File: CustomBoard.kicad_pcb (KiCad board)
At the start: 2 copper layers, 32.9 x 32.8 mm, 25 parts, among them J1 RIGHT, J10 Sensor08, J11 Sensor09, J12 Sensor10, J13 Sensor11, J14 Sensor12, J15 Sensor13, J16 Sensor14, J17 TEST_1P, J2 LEFT, J3 Sensor01, J4 Sensor02, J5 Sensor03, J6 Sensor04, J7 Sensor05, J8 Sensor06, J9 Sensor07, U1 DS28E05, U2 PCA9555

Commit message: 4m range ToF sensor parts
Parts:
- removed G***: OUTLINE, board_outlines:TMP_THICK_BASE

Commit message: new footprints
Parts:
- removed J15: Sensor13, footprint:SensorPads
- removed J16: Sensor14, footprint:SensorPads
- removed J17: TEST_1P, Measurement_Points:Measurement_Point_Round-SMD-Pad_Small
- removed R2, R3: 10k, Resistors_SMD:R_0603
- added C2: 100n, Capacitors_SMD:C_0402, F.Cu at (146.1, 117.6)
- added C3: 4.7u, Capacitors_SMD:C_0402, F.Cu at (151.9, 117.6)
- added R4: 10k, Resistors_SMD:R_0402, F.Cu at (149.0, 112.4)
- added U3: VL53L1X, footprint:VL53L1X, F.Cu at (148.2, 117.6)
- C1: value PowerC -> 100n; footprint Capacitors_SMD:C_0603 -> Capacitors_SMD:C_0402; moved to B.Cu
- D1: footprint LEDs:LED_0603 -> LEDs:LED_0402
- J1: footprint Pin_Headers:Pin_Header_Straight_1x10_Pitch2.00mm_SMD_Pin1Right -> Pin_Header_Straight_1x10_Pitch2.00mm_SMD_Pin1Right; moved to F.Cu
- J2: footprint Pin_Headers:Pin_Header_Straight_1x10_Pitch2.00mm_SMD_Pin1Left -> Pin_Header_Straight_1x10_Pitch2.00mm_SMD_Pin1Left; moved to F.Cu
- R1: footprint Resistors_SMD:R_0603 -> Resistors_SMD:R_0402; moved to B.Cu
- U1, U2: moved to B.Cu
- moved J12 14.6 mm to (165.4, 114.8), turned to 90 degrees
- moved J11 13.6 mm to (165.9, 122.4), turned to 90 degrees
- moved J13 12.5 mm to (165.7, 108.1)
- moved J10 12.2 mm to (161.9, 130.4)
- moved J14 9.84 mm to (162.2, 102.7), turned to 0 degrees
- moved J5 8.35 mm to (132.1, 110.7), turned to 90 degrees
- moved J4 7.30 mm to (135.9, 102.8), turned to 0 degrees
- moved J6 5.70 mm to (132.1, 117.2), turned to 90 degrees
- moved J9 5.45 mm to (148.8, 132.6)
- moved J7 4.40 mm to (132.0, 124.5)
- moved J8 1.57 mm to (136.4, 130.7), turned to 0 degrees
- moved J3 0.86 mm to (150.3, 100.6)
- turned C1 to 90 degrees
- turned R1 to 90 degrees
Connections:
- net WKUP/OW renamed OW
- U2 pad 17: TEST -> S15
- U2 pad 18: Net-(R3-Pad1) -> GND
- U2 pad 22: Net-(R2-Pad1) -> (no net)
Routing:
- net GND: track 126.5 -> 19.4 mm, vias 14 -> 0
- net S01: track 24.5 -> 0.00 mm
- net S13: track 21.3 -> 0.00 mm
- net S03: track 21.0 -> 0.00 mm
- net S02: track 21.0 -> 0.00 mm
- net S14: track 20.2 -> 0.00 mm
- net S10: track 18.8 -> 0.00 mm
- net S06: track 17.3 -> 0.00 mm
- net S07: track 16.3 -> 0.00 mm
- net S04: track 16.3 -> 0.00 mm
- net S09: track 16.2 -> 0.00 mm
- net S11: track 15.7 -> 0.00 mm
- net S12: track 15.6 -> 0.00 mm
- net S05: track 14.8 -> 0.00 mm
- net S08: track 14.1 -> 0.00 mm
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
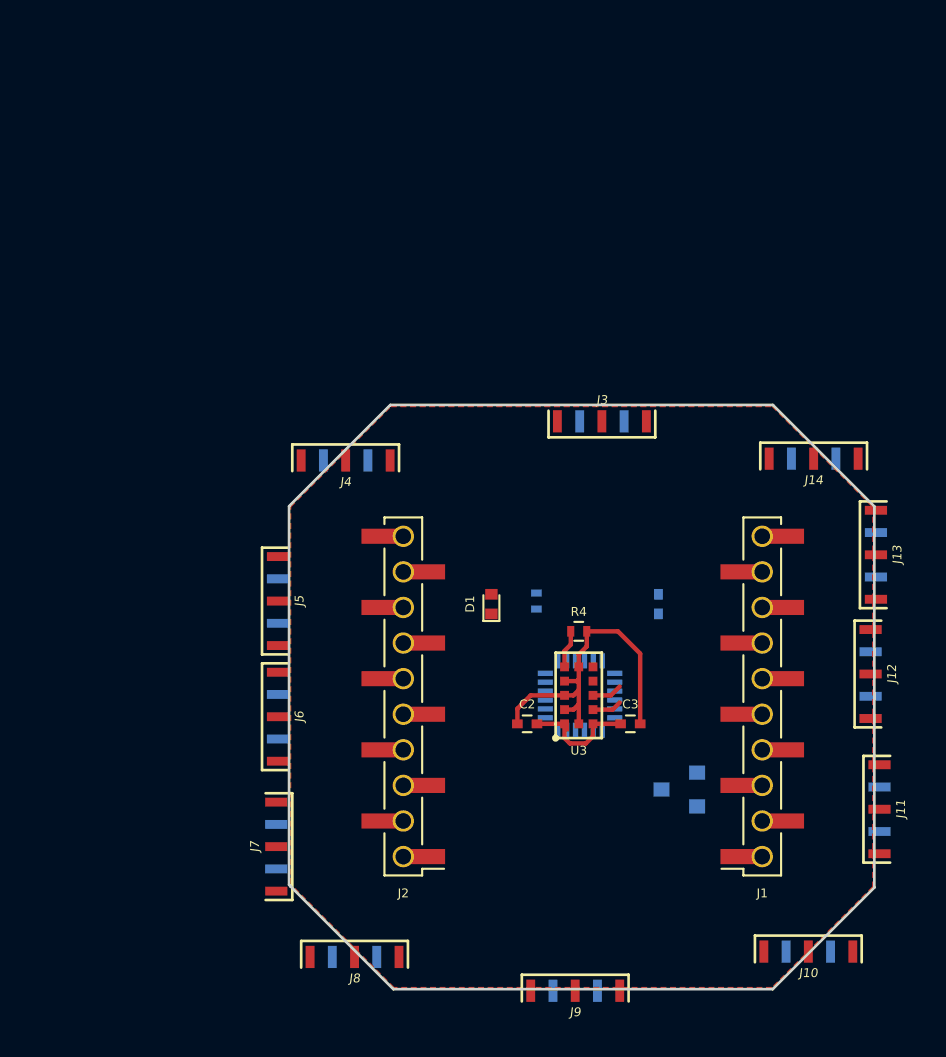
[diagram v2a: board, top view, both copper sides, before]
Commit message: dimensions fixed
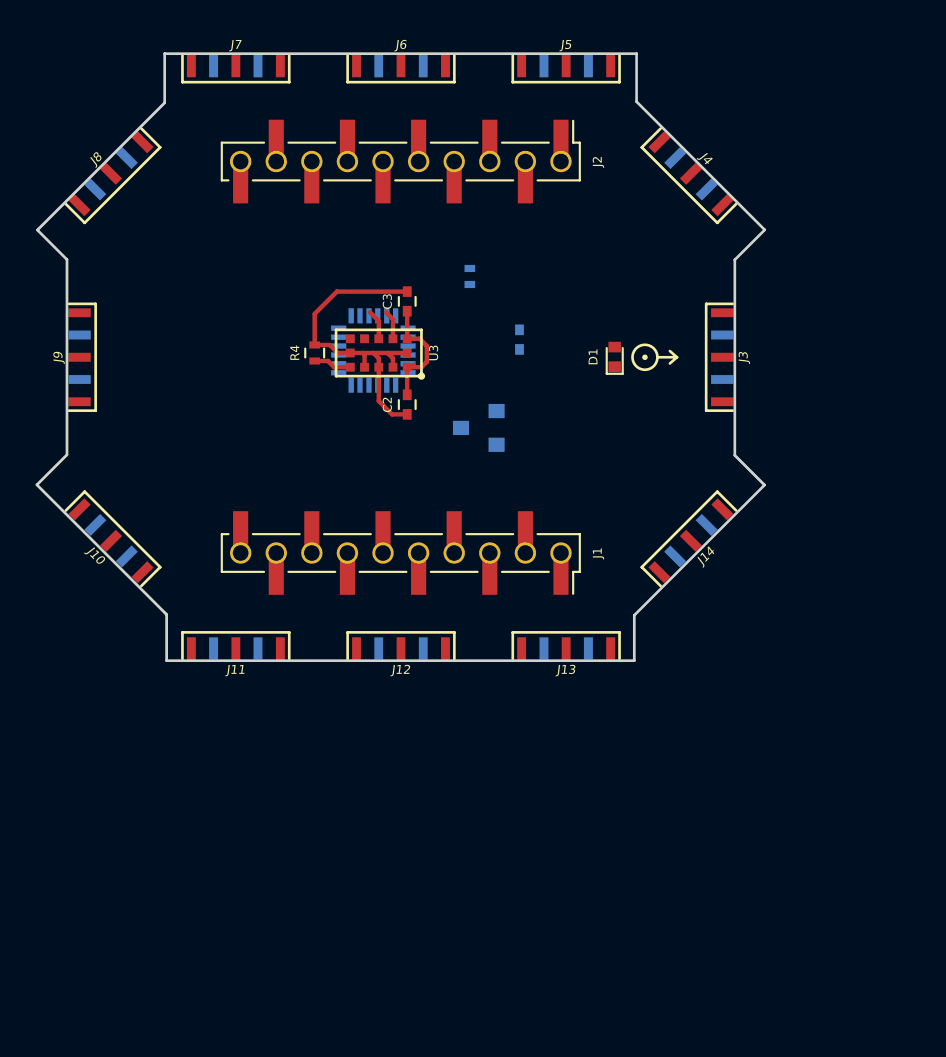
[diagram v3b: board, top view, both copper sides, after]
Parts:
- added EXP_ORIENTATION: VAL**, crazy2libs:EXP_ORIENTATION, F.Cu at (152.7, 97.0)
- moved J8 46.1 mm to (122.7, 86.7), turned to 225 degrees
- moved J10 45.5 mm to (122.7, 107.3), turned to 315 degrees
- moved J9 45.2 mm to (121.0, 97.0), turned to 270 degrees
- moved J7 43.9 mm to (129.7, 80.6), turned to 180 degrees
- moved J11 37.3 mm to (129.7, 113.4), turned to 0 degrees
- moved J6 37.2 mm to (139.0, 80.6), turned to 180 degrees
- moved J5 34.1 mm to (148.3, 80.6), turned to 180 degrees
- moved J2 30.1 mm to (139.0, 86.0), turned to 270 degrees
- moved C3 26.8 mm to (139.4, 93.9), turned to 90 degrees
- moved J12 26.4 mm to (139.0, 113.4), turned to 0 degrees
- moved J4 25.2 mm to (155.3, 86.7), turned to 135 degrees
- moved U1 23.2 mm to (143.4, 101.0)
- moved U2 22.6 mm to (137.5, 96.6)
- moved U3 21.9 mm to (139.4, 97.6), turned to 90 degrees
- moved J1 21.9 mm to (139.0, 108.0), turned to 270 degrees
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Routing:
- removed copper zone on F.Cu, net GND
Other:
- board size 32.9 x 32.8 mm -> 40.9 x 34.1 mm

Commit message: routing started
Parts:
- J1, J2: moved to B.Cu
- moved C1 17.8 mm to (127.9, 95.2), turned to 270 degrees
- moved U1 12.6 mm to (131.0, 102.9), turned to 90 degrees
- moved R1 8.43 mm to (151.0, 94.7), turned to 270 degrees
- moved U2 5.26 mm to (132.2, 97.0), turned to 180 degrees
- turned J1 to 90 degrees
- turned J2 to 90 degrees
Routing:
- net SCL: track 1.67 -> 149.9 mm, vias 0 -> 2
- net SDA: track 1.71 -> 22.0 mm, vias 0 -> 1
- net Net-(D1-Pad1): track 0.00 -> 17.6 mm, vias 0 -> 1
- net S15: track 2.14 -> 13.5 mm, vias 0 -> 1
- net VCC: track 6.49 -> 17.0 mm
- net GND: track 19.4 -> 25.3 mm
- net OW: track 0.00 -> 5.72 mm
- net Net-(D1-Pad2): track 0.00 -> 4.30 mm, vias 0 -> 1

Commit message: routing continues
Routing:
- net SDA: track 22.0 -> 118.1 mm
- net GND: track 25.3 -> 40.7 mm, vias 0 -> 1
- net SCL: track 149.9 -> 154.5 mm
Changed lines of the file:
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@@
   (general
     (links 96)
-    (no_connects 58)
+    (no_connects 53)
     (area 118.474999 79.864999 159.525001 114.125001)
     (thickness 0.8)
     (drawings 18023)
-    (tracks 124)
+    (tracks 157)
     (zones 0)
     (modules 24)
@@
   (gr_line (start 183.551 150.189) (end 175.849 152.992) (layer Eco1.User) (width 0.1))
   (gr_line (start 189.83 144.921) (end 183.551 150.189) (layer Eco1.User) (width 0.1))
+  (segment (start 132.23 80.64) (end 132.23 83.34) (width 0.25) (layer F.Cu) (net 1))
+  (segment (start 130.745 84.825) (end 130 84.825) (width 0.25) (layer B.Cu) (net 1))
+  (segment (start 132.23 83.34) (end 130.745 84.825) (width 0.25) (layer B.Cu) (net 1))
+  (via (at 132.23 83.34) (size 0.6) (drill 0.4) (layers F.Cu B.Cu) (net 1))
+  (segment (start 124.487767 84.922233) (end 124.487767 84.927767) (width 0.25) (layer F.Cu) (net 1))
+  (segment (start 124.487767 84.927767) (end 125.56 86) (width 0.25) (layer F.Cu) (net 1))
+  (segment (start 125.56 86) (end 130 86) (width 0.25) (layer F.Cu) (net 1))
+  (segment (start 130.96 101.88) (end 131.49 101.88) (width 0.25) (layer B.Cu) (net 1))
+  (segment (start 132.46 100.91) (end 132.46 98.9) (width 0.25) (layer B.Cu) (net 1))
+  (segment (start 131.49 101.88) (end 132.46 100.91) (width 0.25) (layer B.Cu) (net 1))
   (segment (start 132.96 95) (end 132.96 93.52) (width 0.25) (layer B.Cu) (net 1))
   (segment (start 133.46 93.51) (end 133.46 95) (width 0.25) (layer B.Cu) (net 1))
@@
   (via (at 149.08 97.54) (size 0.6) (drill 0.4) (layers F.Cu B.Cu) (net 4))
   (segment (start 147.24 95.7) (end 149.08 97.54) (width 0.25) (layer B.Cu) (net 4))
-  (segment (start 137.76 95.96) (end 137.76 95) (width 0.25) (layer F.Cu) (net 5) (status 400000))
+  (segment (start 128.415 108.765) (end 128.415 107.245) (width 0.25) (layer F.Cu) (net 5))
+  (segment (start 128.415 107.245) (end 124.88 103.71) (width 0.25) (layer F.Cu) (net 5))
+  (segment (start 122.72 86.69) (end 124.88 88.85) (width 0.25) (layer F.Cu) (net 5))
+  (segment (start 124.88 88.85) (end 124.88 103.71) (width 0.25) (layer F.Cu) (net 5))
+  (segment (start 129.73 83.67) (end 129.73 80.64) (width 0.25) (layer F.Cu) (net 5))
+  (segment (start 130.45 84.39) (end 129.73 83.67) (width 0.25) (layer F.Cu) (net 5))
+  (segment (start 148.57 84.39) (end 130.45 84.39) (width 0.25) (layer F.Cu) (net 5))
+  (segment (start 149.46 85.28) (end 148.57 84.39) (width 0.25) (layer F.Cu) (net 5))
+  (segment (start 149.46 86.32) (end 149.46 85.28) (width 0.25) (layer F.Cu) (net 5))
+  (segment (start 153.06 89.92) (end 149.46 86.32) (width 0.25) (layer F.Cu) (net 5))
+  (segment (start 153.06 103.48) (end 153.06 89.92) (width 0.25) (layer F.Cu) (net 5))
+  (segment (start 149.63 106.91) (end 153.06 103.48) (width 0.25) (layer F.Cu) (net 5))
+  (segment (start 149.63 108.62) (end 149.63 106.91) (width 0.25) (layer F.Cu) (net 5))
+  (segment (start 148.79 109.46) (end 149.63 108.62) (width 0.25) (layer F.Cu) (net 5))
+  (segment (start 129.11 109.46) (end 148.79 109.46) (width 0.25) (layer F.Cu) (net 5))
+  (segment (start 128.415 108.765) (end 129.11 109.46) (width 0.25) (layer F.Cu) (net 5))
+  (segment (start 122.72 107.31) (end 122.72 107.27) (width 0.25) (layer F.Cu) (net 5))
+  (segment (start 155.3 107.31) (end 155.27 107.31) (width 0.25) (layer F.Cu) (net 5))
+  (segment (start 155.3 86.69) (end 155.29 86.69) (width 0.25) (layer F.Cu) (net 5))
+  (segment (start 137.76 95.96) (end 137.76 95) (width 0.25) (layer F.Cu) (net 5))
   (segment (start 135.62 92.86) (end 135.62 92.09) (width 0.25) (layer B.Cu) (net 5))
   (segment (start 137.25 94.49) (end 135.62 92.86) (width 0.25) (layer B.Cu) (net 5))
@@
   (segment (start 135.62 92.09) (end 132.38 92.09) (width 0.25) (layer B.Cu) (net 5))
   (segment (start 142 89.11) (end 139.02 92.09) (width 0.25) (layer B.Cu) (net 5))
-  (segment (start 138.56 95.96) (end 138.56 94.72) (width 0.25) (layer F.Cu) (net 6) (status 400000))
-  (segment (start 140 92.17) (end 140 86) (width 0.25) (layer F.Cu) (net 6) (status 800000))
+  (segment (start 140 87.175) (end 140 82.74) (width 0.25) (layer B.Cu) (net 6))
+  (segment (start 140 82.74) (end 139.73 82.47) (width 0.25) (layer B.Cu) (net 6))
+  (segment (start 147.04 80.64) (end 147.04 81.84) (width 0.25) (layer B.Cu) (net 6))
+  (segment (start 147.04 81.84) (end 147.67 82.47) (width 0.25) (layer B.Cu) (net 6))
+  (segment (start 137.76 80.64) (end 137.76 82.02) (width 0.25) (layer B.Cu) (net 6))
+  (segment (start 137.76 82.02) (end 138.21 82.47) (width 0.25) (layer B.Cu) (net 6))
+  (segment (start 128.48 80.64) (end 128.48 82.19) (width 0.25) (layer B.Cu) (net 6))
+  (segment (start 148.74 82.47) (end 148.89 82.62) (width 0.25) (layer B.Cu) (net 6))
+  (segment (start 128.76 82.47) (end 138.21 82.47) (width 0.25) (layer B.Cu) (net 6))
+  (segment (start 138.21 82.47) (end 139.73 82.47) (width 0.25) (layer B.Cu) (net 6))
+  (segment (start 139.73 82.47) (end 147.67 82.47) (width 0.25) (layer B.Cu) (net 6))
+  (segment (start 147.67 82.47) (end 148.74 82.47) (width 0.25) (layer B.Cu) (net 6))
+  (segment (start 128.48 82.19) (end 128.76 82.47) (width 0.25) (layer B.Cu) (net 6))
+  (segment (start 157.06 95.75) (end 155.64 95.75) (width 0.25) (layer B.Cu) (net 6))
+  (segment (start 155.64 95.75) (end 155.37 95.48) (width 0.25) (layer B.Cu) (net 6))
+  (segment (start 138.56 95.96) (end 138.56 94.72) (width 0.25) (layer F.Cu) (net 6))
+  (segment (start 140 92.17) (end 140 86) (width 0.25) (layer F.Cu) (net 6))
   (via (at 140 92.17) (size 0.6) (drill 0.4) (layers F.Cu B.Cu) (net 6))
   (segment (start 140 92.84) (end 140 92.17) (width 0.25) (layer B.Cu) (net 6))
@@
   (segment (start 156.183883 106.426117) (end 156.166117 106.426117) (width 0.25) (layer B.Cu) (net 6))
   (segment (start 156.166117 106.426117) (end 154.89 105.15) (width 0.25) (layer B.Cu) (net 6))
-  (segment (start 157.06 95.75) (end 155.64 95.75) (width 0.25) (layer B.Cu) (net 6))
-  (segment (start 155.64 95.75) (end 155.37 95.48) (width 0.25) (layer B.Cu) (net 6))
   (segment (start 154.416117 85.806117) (end 154.413883 85.806117) (width 0.25) (layer B.Cu) (net 6))
   (segment (start 154.413883 85.806117) (end 153.245 86.975) (width 0.25) (layer B.Cu) (net 6))
-  (segment (start 147.04 80.64) (end 147.04 82.24) (width 0.25) (layer B.Cu) (net 6))
-  (segment (start 147.04 82.24) (end 147.42 82.62) (width 0.25) (layer B.Cu) (net 6))
-  (segment (start 137.76 80.64) (end 137.76 82.19) (width 0.25) (layer B.Cu) (net 6))
-  (segment (start 137.76 82.19) (end 138.19 82.62) (width 0.25) (layer B.Cu) (net 6))
   (segment (start 120.95 98.25) (end 122.51 98.25) (width 0.25) (layer B.Cu) (net 6))
   (segment (start 122.51 98.25) (end 122.68 98.42) (width 0.25) (layer B.Cu) (net 6))
   (segment (start 123.603883 108.193883) (end 123.603883 108.186117) (width 0.25) (layer B.Cu) (net 6))
   (segment (start 123.603883 108.186117) (end 124.83 106.96) (width 0.25) (layer B.Cu) (net 6))
-  (segment (start 128.48 80.64) (end 128.48 82.25) (width 0.25) (layer B.Cu) (net 6))
   (segment (start 122.68 88.417766) (end 121.836117 87.573883) (width 0.25) (layer B.Cu) (net 6))
   (segment (start 122.68 104.81) (end 122.68 98.42) (width 0.25) (layer B.Cu) (net 6))
@@
   (segment (start 148.89 82.62) (end 153.245 86.975) (width 0.25) (layer B.Cu) (net 6))
   (segment (start 153.245 86.975) (end 155.37 89.1) (width 0.25) (layer B.Cu) (net 6))
-  (segment (start 128.85 82.62) (end 138.19 82.62) (width 0.25) (layer B.Cu) (net 6))
-  (segment (start 138.19 82.62) (end 147.42 82.62) (width 0.25) (layer B.Cu) (net 6))
-  (segment (start 147.42 82.62) (end 148.89 82.62) (width 0.25) (layer B.Cu) (net 6))
-  (segment (start 128.48 82.25) (end 128.85 82.62) (width 0.25) (layer B.Cu) (net 6))
   (segment (start 130.96 95) (end 130.96 92.69) (width 0.25) (layer B.Cu) (net 6))
   (segment (start 140 90.15) (end 140 86) (width 0.25) (layer B.Cu) (net 6))
@@
   (segment (start 134 104.72) (end 134 108) (width 0.25) (layer B.Cu) (net 21))
   (segment (start 133.16 103.88) (end 134 104.72) (width 0.25) (layer B.Cu) (net 21))
-  (segment (start 130.26 96.2) (end 128.81 96.2) (width 0.25) (layer B.Cu) (net 22) (status 400000))
-  (segment (start 133.64 97.21) (end 134.16 97.21) (width 0.25) (layer F.Cu) (net 22) (status 800000))
+  (segment (start 130.26 96.2) (end 128.81 96.2) (width 0.25) (layer B.Cu) (net 22))
+  (segment (start 133.64 97.21) (end 134.16 97.21) (width 0.25) (layer F.Cu) (net 22))
   (segment (start 132.63 96.2) (end 133.64 97.21) (width 0.25) (layer F.Cu) (net 22))
   (segment (start 127.53 96.2) (end 132.63 96.2) (width 0.25) (layer F.Cu) (net 22))

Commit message: routing optimization
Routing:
- net VCC: track 17.0 -> 99.8 mm, vias 0 -> 21
- net GND: track 40.7 -> 118.5 mm, vias 1 -> 22
- net SDA: track 118.1 -> 160.3 mm
- net S07: track 0.00 -> 17.7 mm, vias 0 -> 4
- net (no net): track 0.00 -> 8.30 mm, vias 0 -> 4
- net SCL: track 154.5 -> 152.9 mm
- added copper zone on F.Cu, net GND
- added copper zone on B.Cu, net VCC
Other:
- rule trace_min: 0.2 -> 0.1

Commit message: modifications
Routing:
- net VCC: track 99.8 -> 94.6 mm, vias 21 -> 19
- net (no net): track 8.30 -> 13.5 mm, vias 4 -> 6
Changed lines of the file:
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@@
   (general
     (links 96)
-    (no_connects 12)
-    (area 118.474999 79.864999 159.525001 114.125001)
+    (no_connects 13)
+    (area 82.600999 40.959499 195.401001 153.042001)
     (thickness 0.8)
     (drawings 18023)
@@
   (via (at 127.21 100.93) (size 0.6) (drill 0.4) (layers F.Cu B.Cu) (net 0))
   (segment (start 127.18 100.9) (end 127.21 100.93) (width 0.25) (layer B.Cu) (net 0))
+  (segment (start 125.6 94.63) (end 125.7 94.63) (width 0.25) (layer B.Cu) (net 0))
+  (via (at 125.74 99.69) (size 0.6) (drill 0.4) (layers F.Cu B.Cu) (net 0))
+  (segment (start 125.74 94.75) (end 125.74 99.69) (width 0.25) (layer F.Cu) (net 0))
+  (segment (start 125.76 94.73) (end 125.74 94.75) (width 0.25) (layer F.Cu) (net 0))
+  (via (at 125.76 94.73) (size 0.6) (drill 0.4) (layers F.Cu B.Cu) (net 0))
+  (segment (start 125.76 94.69) (end 125.76 94.73) (width 0.25) (layer B.Cu) (net 0))
+  (segment (start 125.7 94.63) (end 125.76 94.69) (width 0.25) (layer B.Cu) (net 0))
   (segment (start 136.51 113.36) (end 136.51 110.52) (width 0.25) (layer F.Cu) (net 1))
   (via (at 138.03 105.91) (size 0.6) (drill 0.4) (layers F.Cu B.Cu) (net 1))
@@
   (segment (start 135.46 96.76) (end 136.16 96.76) (width 0.25) (layer F.Cu) (net 1))
   (segment (start 135.01 96.31) (end 135.46 96.76) (width 0.25) (layer F.Cu) (net 1))
-  (segment (start 125.6 94.63) (end 125.7 94.63) (width 0.25) (layer B.Cu) (net 2))
-  (via (at 125.74 99.69) (size 0.6) (drill 0.4) (layers F.Cu B.Cu) (net 2))
-  (segment (start 125.74 94.75) (end 125.74 99.69) (width 0.25) (layer F.Cu) (net 2))
-  (segment (start 125.76 94.73) (end 125.74 94.75) (width 0.25) (layer F.Cu) (net 2))
-  (via (at 125.76 94.73) (size 0.6) (drill 0.4) (layers F.Cu B.Cu) (net 2))
-  (segment (start 125.76 94.69) (end 125.76 94.73) (width 0.25) (layer B.Cu) (net 2))
-  (segment (start 125.7 94.63) (end 125.76 94.69) (width 0.25) (layer B.Cu) (net 2))
   (segment (start 138.49 90.45) (end 132.39 90.45) (width 0.25) (layer F.Cu) (net 2))
   (segment (start 138.5 90.44) (end 138.49 90.45) (width 0.25) (layer F.Cu) (net 2))
